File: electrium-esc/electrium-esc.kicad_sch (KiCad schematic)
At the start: 29 parts, among them J2 USB_MICRO, J3 Conn_01x04_Male, J4 Conn_01x03_Male, J5 Conn_01x04_Male

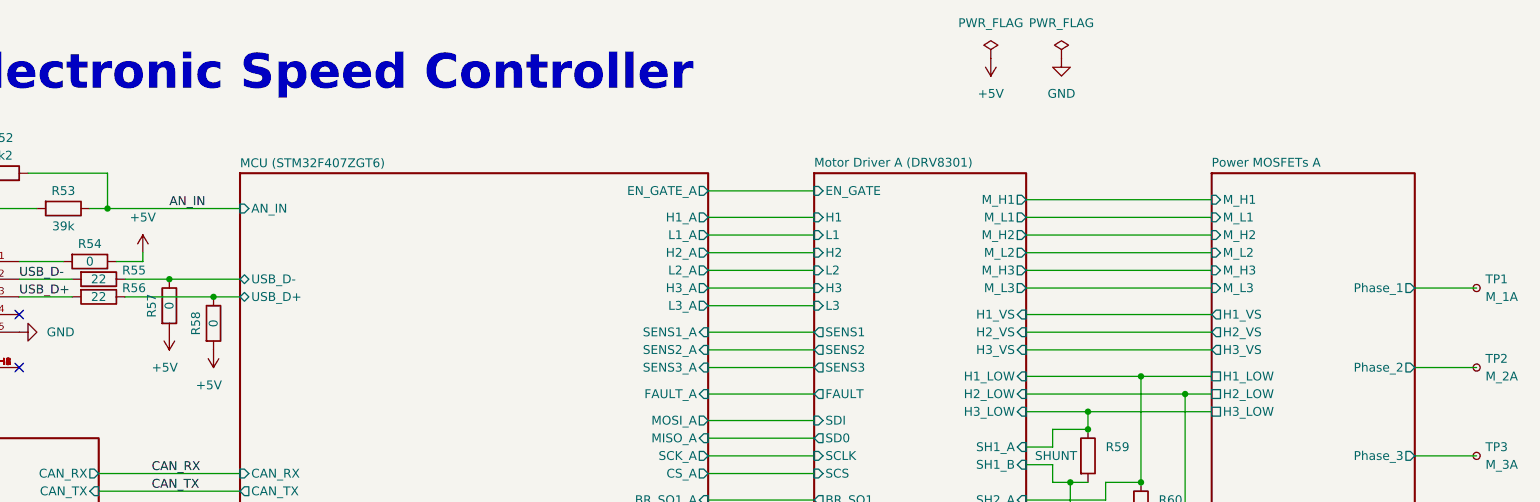
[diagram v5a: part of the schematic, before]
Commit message: Add power caps
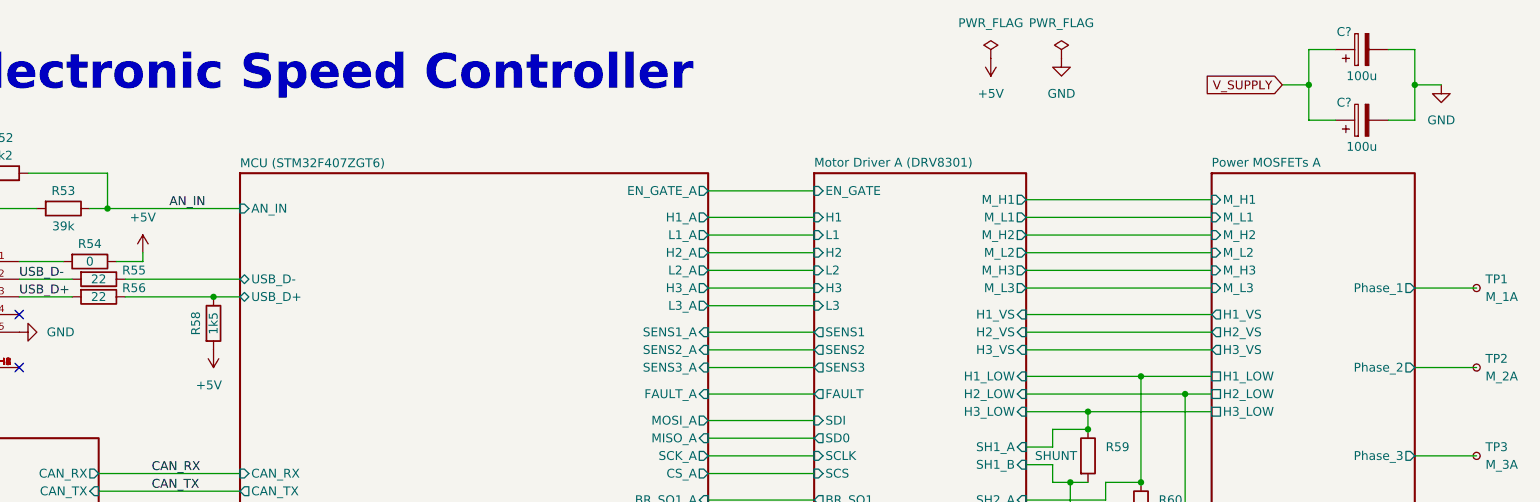
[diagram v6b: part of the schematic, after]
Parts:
- removed R57: 0, Resistor_SMD:R_0603_1608Metric, symbol Device:R
- added C? (x2): 100u, symbol Device:C_Polarized
- R58: value 0 -> 1k5
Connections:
- net GND: now also C?.2, C?.2
- net V_SUPPLY: now also C?.1, C?.1
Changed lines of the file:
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@@
   (junction (at 71.12 168.91) (diameter 0) (color 0 0 0 0)
   )
+  (junction (at 238.76 25.4) (diameter 0) (color 0 0 0 0)
+  )
   (junction (at 214.63 90.17) (diameter 0) (color 0 0 0 0)
   )
@@
   (junction (at 78.74 161.29) (diameter 0) (color 0 0 0 0)
   )
+  (junction (at 254 25.4) (diameter 0) (color 0 0 0 0)
+  )
   (junction (at 81.28 55.88) (diameter 0) (color 0 0 0 0)
   )
@@
   )
   (junction (at 220.98 132.08) (diameter 0) (color 0 0 0 0)
-  )
-  (junction (at 74.93 53.34) (diameter 0) (color 0 0 0 0)
   )
   (junction (at 66.04 43.18) (diameter 0) (color 0 0 0 0)
@@
     (stroke (width 0) (type default) (color 0 0 0 0))
   )
+  (wire (pts (xy 250.19 20.32) (xy 254 20.32))
+    (stroke (width 0) (type default) (color 0 0 0 0))
+  )
   (wire (pts (xy 198.12 125.73) (xy 226.06 125.73))
     (stroke (width 0) (type default) (color 0 0 0 0))
@@
     (stroke (width 0) (type default) (color 0 0 0 0))
   )
+  (wire (pts (xy 234.95 25.4) (xy 238.76 25.4))
+    (stroke (width 0) (type default) (color 0 0 0 0))
+  )
   (wire (pts (xy 66.04 43.18) (xy 63.5 43.18))
     (stroke (width 0) (type default) (color 0 0 0 0))
@@
     (stroke (width 0) (type default) (color 0 0 0 0))
   )
+  (wire (pts (xy 238.76 20.32) (xy 242.57 20.32))
+    (stroke (width 0) (type default) (color 0 0 0 0))
+  )
   (wire (pts (xy 220.98 69.85) (xy 224.79 69.85))
     (stroke (width 0) (type default) (color 0 0 0 0))
   )
+  (wire (pts (xy 254 25.4) (xy 257.81 25.4))
+    (stroke (width 0) (type default) (color 0 0 0 0))
+  )
   (wire (pts (xy 207.01 134.62) (xy 207.01 137.16))
     (stroke (width 0) (type default) (color 0 0 0 0))
@@
     (stroke (width 0) (type default) (color 0 0 0 0))
   )
-  (wire (pts (xy 68.58 53.34) (xy 74.93 53.34))
-    (stroke (width 0) (type default) (color 0 0 0 0))
-  )
   (wire (pts (xy 198.12 67.31) (xy 214.63 67.31))
     (stroke (width 0) (type default) (color 0 0 0 0))
@@
     (stroke (width 0) (type default) (color 0 0 0 0))
   )
-  (wire (pts (xy 74.93 53.34) (xy 85.09 53.34))
+  (wire (pts (xy 68.58 53.34) (xy 85.09 53.34))
     (stroke (width 0) (type default) (color 0 0 0 0))
   )
@@
     (stroke (width 0) (type default) (color 0 0 0 0))
   )
+  (wire (pts (xy 238.76 25.4) (xy 238.76 30.48))
+    (stroke (width 0) (type default) (color 0 0 0 0))
+  )
+  (wire (pts (xy 254 20.32) (xy 254 25.4))
+    (stroke (width 0) (type default) (color 0 0 0 0))
+  )
   (wire (pts (xy 209.55 90.17) (xy 214.63 90.17))
     (stroke (width 0) (type default) (color 0 0 0 0))
@@
     (stroke (width 0) (type default) (color 0 0 0 0))
   )
+  (wire (pts (xy 254 25.4) (xy 254 30.48))
+    (stroke (width 0) (type default) (color 0 0 0 0))
+  )
   (wire (pts (xy 198.12 63.5) (xy 224.79 63.5))
     (stroke (width 0) (type default) (color 0 0 0 0))
@@
     (stroke (width 0) (type default) (color 0 0 0 0))
   )
+  (wire (pts (xy 238.76 25.4) (xy 238.76 20.32))
+    (stroke (width 0) (type default) (color 0 0 0 0))
+  )
   (wire (pts (xy 198.12 60.96) (xy 224.79 60.96))
     (stroke (width 0) (type default) (color 0 0 0 0))
@@
     (stroke (width 0) (type default) (color 0 0 0 0))
   )
+  (wire (pts (xy 254 30.48) (xy 250.19 30.48))
+    (stroke (width 0) (type default) (color 0 0 0 0))
+  )
   (wire (pts (xy 152.4 125.73) (xy 167.64 125.73))
     (stroke (width 0) (type default) (color 0 0 0 0))
@@
   )
   (wire (pts (xy 152.4 147.32) (xy 167.64 147.32))
+    (stroke (width 0) (type default) (color 0 0 0 0))
+  )
+  (wire (pts (xy 238.76 30.48) (xy 242.57 30.48))
     (stroke (width 0) (type default) (color 0 0 0 0))
   )
@@
   (label "USB_D+" (at 53.34 55.88 0)
     (effects (font (size 1.27 1.27)) (justify left bottom))
+  )
+  (global_label "V_SUPPLY" (shape input) (at 234.95 25.4 180) (fields_autoplaced)
+    (effects (font (size 1.27 1.27)) (justify right))
+    (property "Intersheet References" "${INTERSHEET_REFS}" (id 0) (at 223.284 25.3206 0)
+      (effects (font (size 1.27 1.27)) (justify right) hide)
+    )
   )
   (global_label "V_SUPPLY" (shape input) (at 43.18 43.18 180) (fields_autoplaced)
@@
     (pin "1")
   )
-  (symbol (lib_id "power:+5V") (at 74.93 60.96 180) (unit 1)
-    (in_bom yes) (on_board yes)
-    (property "Reference" "#PWR054" (id 0) (at 74.93 57.15 0)
-      (effects (font (size 1.27 1.27)) hide)
-    )
-    (property "Value" "+5V" (id 1) (at 72.39 66.04 0)
-      (effects (font (size 1.27 1.27)) (justify right))
-    )
-    (property "Footprint" "" (id 2) (at 74.93 60.96 0)
-      (effects (font (size 1.27 1.27)) hide)
-    )
-    (property "Datasheet" "" (id 3) (at 74.93 60.96 0)
-      (effects (font (size 1.27 1.27)) hide)
-    )
-    (pin "1")
-  )
   (symbol (lib_id "Device:R") (at 207.01 78.74 0) (unit 1)
     (in_bom yes) (on_board yes)
@@
     )
     (pin "1")
-  )
-  (symbol (lib_id "Device:R") (at 74.93 57.15 0) (unit 1)
-    (in_bom yes) (on_board yes)
-    (property "Reference" "R57" (id 0) (at 72.39 57.15 90))
-    (property "Value" "0" (id 1) (at 74.93 57.15 90))
-    (property "Footprint" "Resistor_SMD:R_0603_1608Metric" (id 2) (at 73.152 57.15 90)
-      (effects (font (size 1.27 1.27)) hide)
-    )
-    (property "Datasheet" "~" (id 3) (at 74.93 57.15 0)
-      (effects (font (size 1.27 1.27)) hide)
-    )
-    (pin "1")
-    (pin "2")
   )
   (symbol (lib_id "Device:R") (at 59.69 43.18 270) (unit 1)
@@
     (pin "1")
   )
+  (symbol (lib_id "Device:C_Polarized") (at 246.38 30.48 90) (unit 1)
+    (in_bom yes) (on_board yes)
+    (property "Reference" "C?" (id 0) (at 243.84 27.94 90))
+    (property "Value" "100u" (id 1) (at 246.38 34.29 90))
+    (property "Footprint" "" (id 2) (at 250.19 29.5148 0)
+      (effects (font (size 1.27 1.27)) hide)
+    )
+    (property "Datasheet" "~" (id 3) (at 246.38 30.48 0)
+      (effects (font (size 1.27 1.27)) hide)
+    )
+    (pin "1")
+    (pin "2")
+  )
   (symbol (lib_id "Connector:TestPoint_Small") (at 262.89 116.84 0) (unit 1)
     (in_bom yes) (on_board yes) (fields_autoplaced)
@@
     (in_bom yes) (on_board yes)
     (property "Reference" "R58" (id 0) (at 78.74 59.69 90))
-    (property "Value" "0" (id 1) (at 81.28 59.69 90))
+    (property "Value" "1k5" (id 1) (at 81.28 59.69 90))
     (property "Footprint" "Resistor_SMD:R_0603_1608Metric" (id 2) (at 79.502 59.69 90)
       (effects (font (size 1.27 1.27)) hide)
@@
     (pin "2")
   )
+  (symbol (lib_id "power:GND") (at 257.81 25.4 0) (unit 1)
+    (in_bom yes) (on_board yes) (fields_autoplaced)
+    (property "Reference" "#PWR?" (id 0) (at 257.81 31.75 0)
+      (effects (font (size 1.27 1.27)) hide)
+    )
+    (property "Value" "GND" (id 1) (at 257.81 30.48 0))
+    (property "Footprint" "" (id 2) (at 257.81 25.4 0)
+      (effects (font (size 1.27 1.27)) hide)
+    )
+    (property "Datasheet" "" (id 3) (at 257.81 25.4 0)
+      (effects (font (size 1.27 1.27)) hide)
+    )
+    (pin "1")
+  )
   (symbol (lib_id "Device:R") (at 50.8 38.1 90) (unit 1)
     (in_bom yes) (on_board yes)
@@
     )
     (property "Datasheet" "~" (id 3) (at 39.37 171.45 0)
+      (effects (font (size 1.27 1.27)) hide)
+    )
+    (pin "1")
+    (pin "2")
+  )
+  (symbol (lib_id "Device:C_Polarized") (at 246.38 20.32 90) (unit 1)
+    (in_bom yes) (on_board yes)
+    (property "Reference" "C?" (id 0) (at 243.84 17.78 90))
+    (property "Value" "100u" (id 1) (at 246.38 24.13 90))
+    (property "Footprint" "" (id 2) (at 250.19 19.3548 0)
+      (effects (font (size 1.27 1.27)) hide)
+    )
+    (property "Datasheet" "~" (id 3) (at 246.38 20.32 0)
       (effects (font (size 1.27 1.27)) hide)
     )
@@
       (reference "#PWR053") (unit 1) (value "GND") (footprint "")
     )
-    (path "/0b384396-2b4c-4bcf-b5ea-c96887cd1130"
-      (reference "#PWR054") (unit 1) (value "+5V") (footprint "")
-    )
     (path "/e3494083-3e75-4d07-bb19-b421b9e5d3f0"
       (reference "#PWR055") (unit 1) (value "+5V") (footprint "")
@@
       (reference "#PWR077") (unit 1) (value "GND") (footprint "")
     )
+    (path "/87338a8a-77b3-496a-a789-31b5c9b51baf"
+      (reference "#PWR?") (unit 1) (value "GND") (footprint "")
+    )
     (path "/95515899-f309-4706-b478-ef0c1d74de3d/6e926fcb-bc57-4a6a-ac9a-7920661fd921"
       (reference "C1") (unit 1) (value "4.7u") (footprint "Capacitor_SMD:C_0603_1608Metric")
@@
       (reference "C77") (unit 1) (value "2.2u") (footprint "Capacitor_SMD:C_0603_1608Metric")
     )
+    (path "/49d1a796-871b-4fe2-9503-f16f11030f78"
+      (reference "C?") (unit 1) (value "100u") (footprint "")
+    )
+    (path "/c476a5aa-d471-4bfa-bd3d-9f9dd6e58542"
+      (reference "C?") (unit 1) (value "100u") (footprint "")
+    )
     (path "/4dcd2554-0c0c-4fca-b220-d2fb156d9cf9/2194da5e-abcb-490c-ad12-09330a88057c"
       (reference "D1") (unit 1) (value "1N5819") (footprint "Diode_THT:D_DO-41_SOD81_P10.16mm_Horizontal")
@@
       (reference "R56") (unit 1) (value "22") (footprint "Resistor_SMD:R_0603_1608Metric")
     )
-    (path "/1659c7ac-4d2e-45e4-a5c9-1f7a880463c6"
-      (reference "R57") (unit 1) (value "0") (footprint "Resistor_SMD:R_0603_1608Metric")
-    )
     (path "/51252bf1-9e93-479b-bc04-9cf3da5bcd58"
-      (reference "R58") (unit 1) (value "0") (footprint "Resistor_SMD:R_0603_1608Metric")
+      (reference "R58") (unit 1) (value "1k5") (footprint "Resistor_SMD:R_0603_1608Metric")
     )
     (path "/0d76d2ab-30c8-46af-9b66-78611601234d"

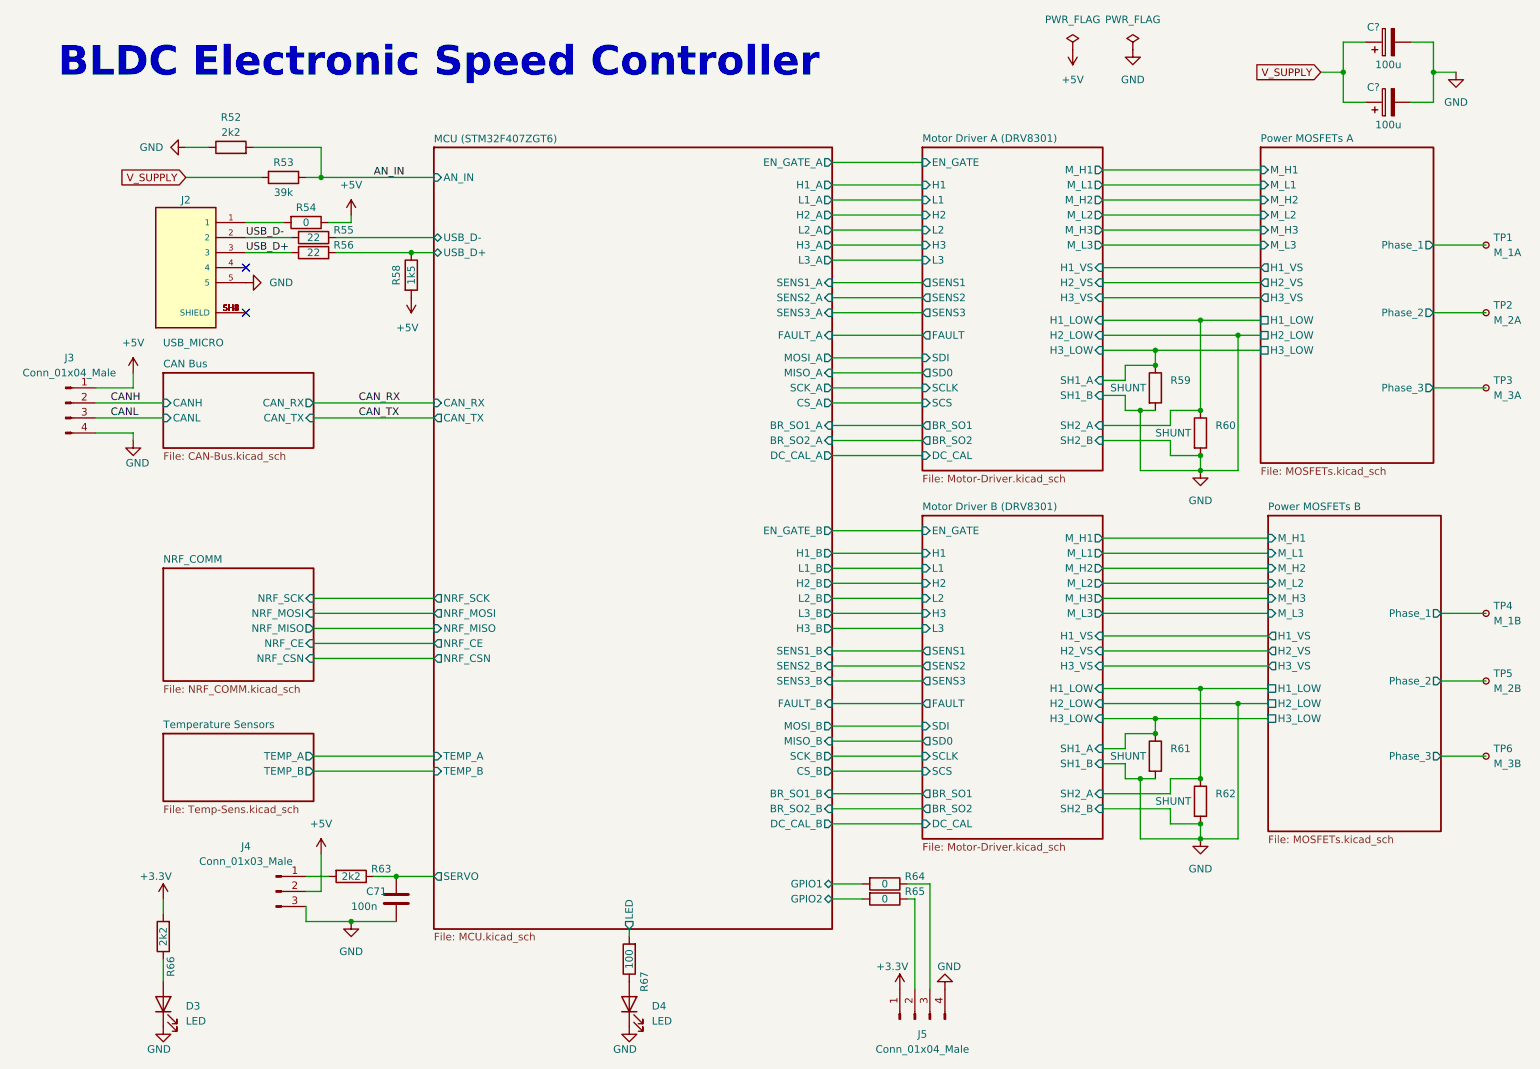
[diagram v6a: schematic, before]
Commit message: add all additional design changes (good to go)
Note: may need to change some footprints depending on what's available
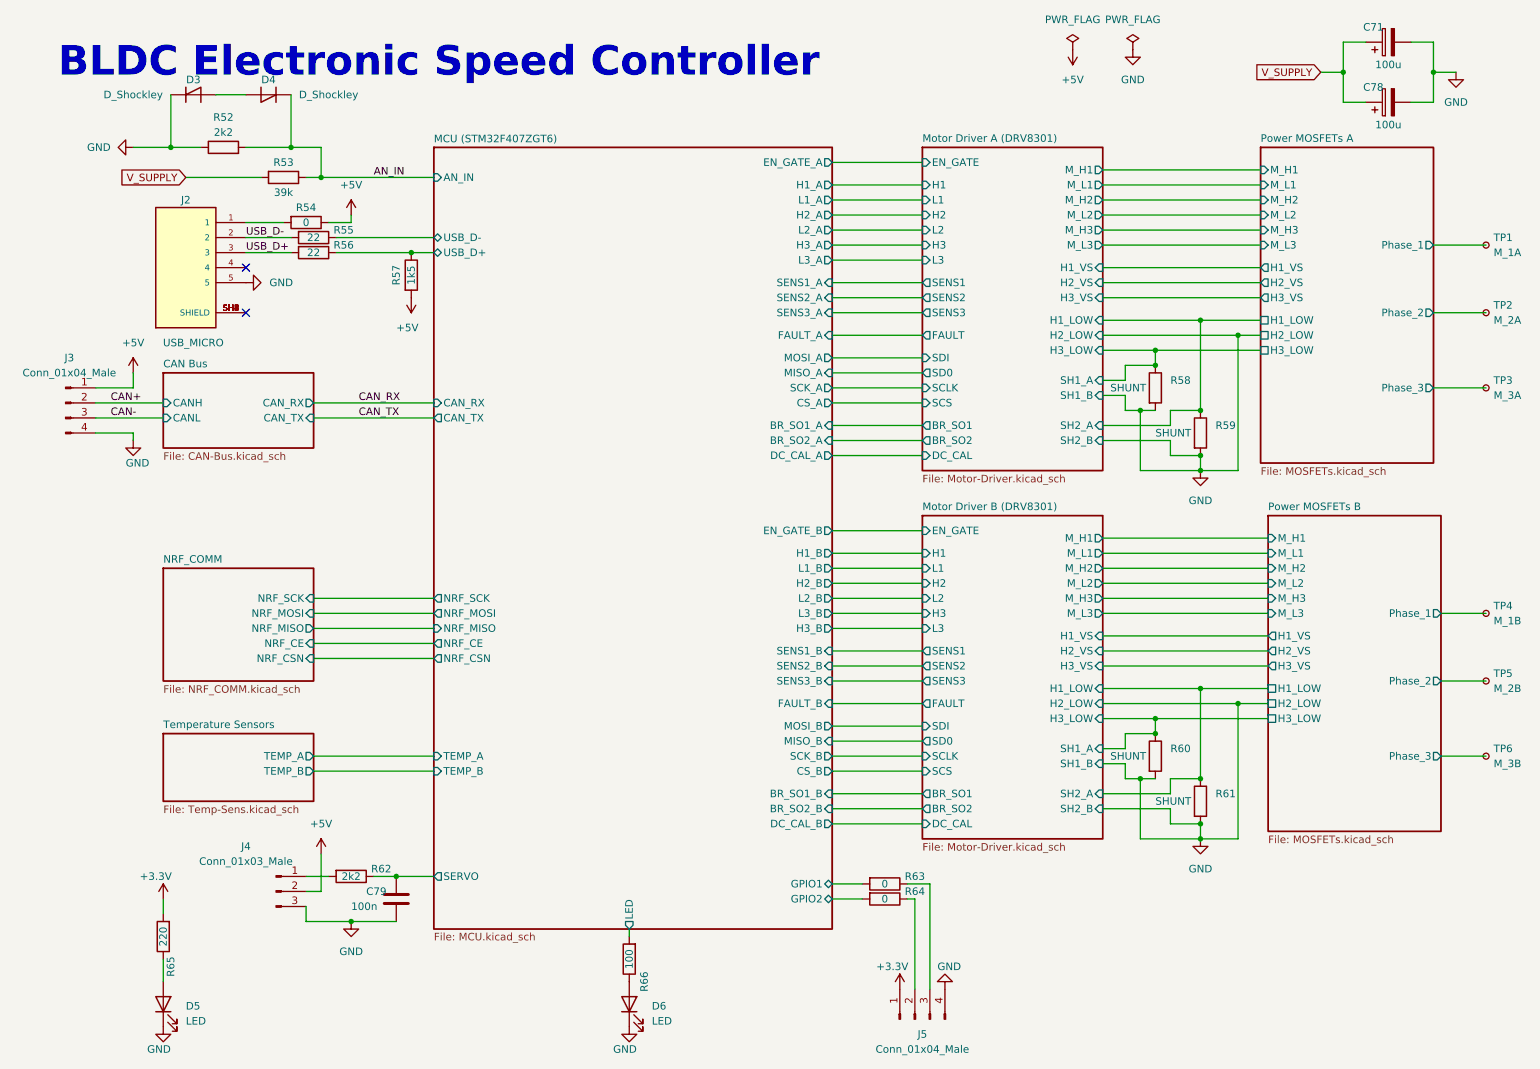
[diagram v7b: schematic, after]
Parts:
- added D3, D4: D_Shockley, Diode_SMD:D_0603_1608Metric, symbol Device:D_Shockley
- R65: renamed from R66; value 2k2 -> 220
- gave numbers to parts that had none: 2
- renumbered C71 to C79, D3 to D5, D4 to D6, R58 to R57, R59 to R58, R60 to R59, R61 to R60, R62 to R61, R63 to R62, R64 to R63, R65 to R64, R67 to R66
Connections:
- net AN_IN: now also D4.1 (K)
- net GND: now also D3.1 (K)
- net CANH renamed CAN+
- net CANL renamed CAN-
- new net: D3.2 (A), D4.2 (A)
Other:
- moved on the sheet: R52

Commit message: final version (good to go!)
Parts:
- C71, C78: value 100u -> 1000u
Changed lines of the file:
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@@
     (in_bom yes) (on_board yes)
     (property "Reference" "C78" (id 0) (at 243.84 27.94 90))
-    (property "Value" "100u" (id 1) (at 246.38 34.29 90))
+    (property "Value" "1000u" (id 1) (at 246.38 34.29 90))
     (property "Footprint" "" (id 2) (at 250.19 29.5148 0)
       (effects (font (size 1.27 1.27)) hide)
@@
     (in_bom yes) (on_board yes)
     (property "Reference" "C71" (id 0) (at 243.84 17.78 90))
-    (property "Value" "100u" (id 1) (at 246.38 24.13 90))
+    (property "Value" "1000u" (id 1) (at 246.38 24.13 90))
     (property "Footprint" "" (id 2) (at 250.19 19.3548 0)
       (effects (font (size 1.27 1.27)) hide)
@@
     )
     (path "/c476a5aa-d471-4bfa-bd3d-9f9dd6e58542"
-      (reference "C71") (unit 1) (value "100u") (footprint "")
+      (reference "C71") (unit 1) (value "1000u") (footprint "")
     )
     (path "/f169605c-998e-4bf3-977e-b281c665fab8/61e8be5d-141d-4f7d-9709-fb6624103054"
@@
     )
     (path "/49d1a796-871b-4fe2-9503-f16f11030f78"
-      (reference "C78") (unit 1) (value "100u") (footprint "")
+      (reference "C78") (unit 1) (value "1000u") (footprint "")
     )
     (path "/5e9c9536-b4af-4c8c-9511-f89016d638a9"
